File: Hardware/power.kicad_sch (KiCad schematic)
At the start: 0 parts

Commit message: CSG325?
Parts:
- added U2: XC7A35T-CSG325, Package_BGA:Xilinx_CSG325, symbol FPGA_Xilinx_Artix7:XC7A35T-CSG325

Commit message: Found the global labels
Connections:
- net GND: now reaches U2.A1 (GND)
- net GND: now also U2.A11 (GND), U2.A18 (GND), U2.A5 (GND), U2.A7 (GND), U2.A8 (GND), U2.B18 (GND), U2.B3 (GND), U2.B7 (GND), U2.B8 (GND), U2.C15 (GND), U2.C2 (GND), U2.C6 (GND), U2.C7 (GND), U2.D12 (GND), U2.D3 (GND), U2.D4 (GND), U2.D7 (GND), U2.E2 (GND), U2.E6 (GND), U2.E7 (GND), U2.E9 (GND), U2.F10 (GND), U2.F16 (GND), U2.F4 (GND), U2.F6 (GND), U2.G1 (GND), U2.G11 (GND), U2.G13 (GND), U2.G5 (GND), U2.G6 (GND), U2.G7 (GND), U2.G9 (GND), U2.H10 (GND), U2.H12 (GND), U2.H3 (GND), U2.H4 (GND), U2.H5 (GND), U2.H6 (GND), U2.H8 (GND), U2.J1 (GND), U2.J11 (GND), U2.J13 (GND), U2.J17 (GND), U2.J2 (GND), U2.J3 (GND), U2.J7 (GND), U2.J9 (GNDADC_0), U2.K12 (GND), U2.K14 (GND), U2.K4 (GND), U2.K8 (GND), U2.L1 (GND), U2.L11 (GND), U2.L13 (GND), U2.L7 (GND), U2.M12 (GND), U2.M18 (GND), U2.M8 (GND), U2.N11 (GND), U2.N13 (GND), U2.N15 (GND), U2.N5 (GND), U2.N7 (GND), U2.N9 (GND), U2.P12 (GND), U2.P2 (GND), U2.P8 (GND), U2.R9 (GND), U2.T16 (GND), U2.T6 (GND), U2.U13 (GND), U2.U3 (GND), U2.V1 (GND), U2.V10 (GND), U2.V18 (GND)
- net +1V8: now reaches U2.E11 (VCCBATT_0)
- net +1V8: now also U2.G12 (VCCAUX), U2.H13 (VCCAUX), U2.J10 (VCCADC_0), U2.K13 (VCCAUX), U2.M13 (VCCAUX), U2.P13 (VCCAUX)
- net +1V0: now reaches U2.F11 (VCCBRAM)
- net +1V0: now also U2.F7 (VCCINT), U2.F9 (VCCINT), U2.G10 (VCCBRAM), U2.G8 (VCCINT), U2.H11 (VCCBRAM), U2.H7 (VCCINT), U2.H9 (VCCINT), U2.J12 (VCCINT), U2.J8 (VCCINT), U2.K11 (VCCINT), U2.K7 (VCCINT), U2.L12 (VCCINT), U2.L8 (VCCINT), U2.M11 (VCCINT), U2.M7 (VCCINT), U2.N10 (VCCINT), U2.N12 (VCCINT), U2.N8 (VCCINT), U2.P11 (VCCINT), U2.P9 (VCCINT)

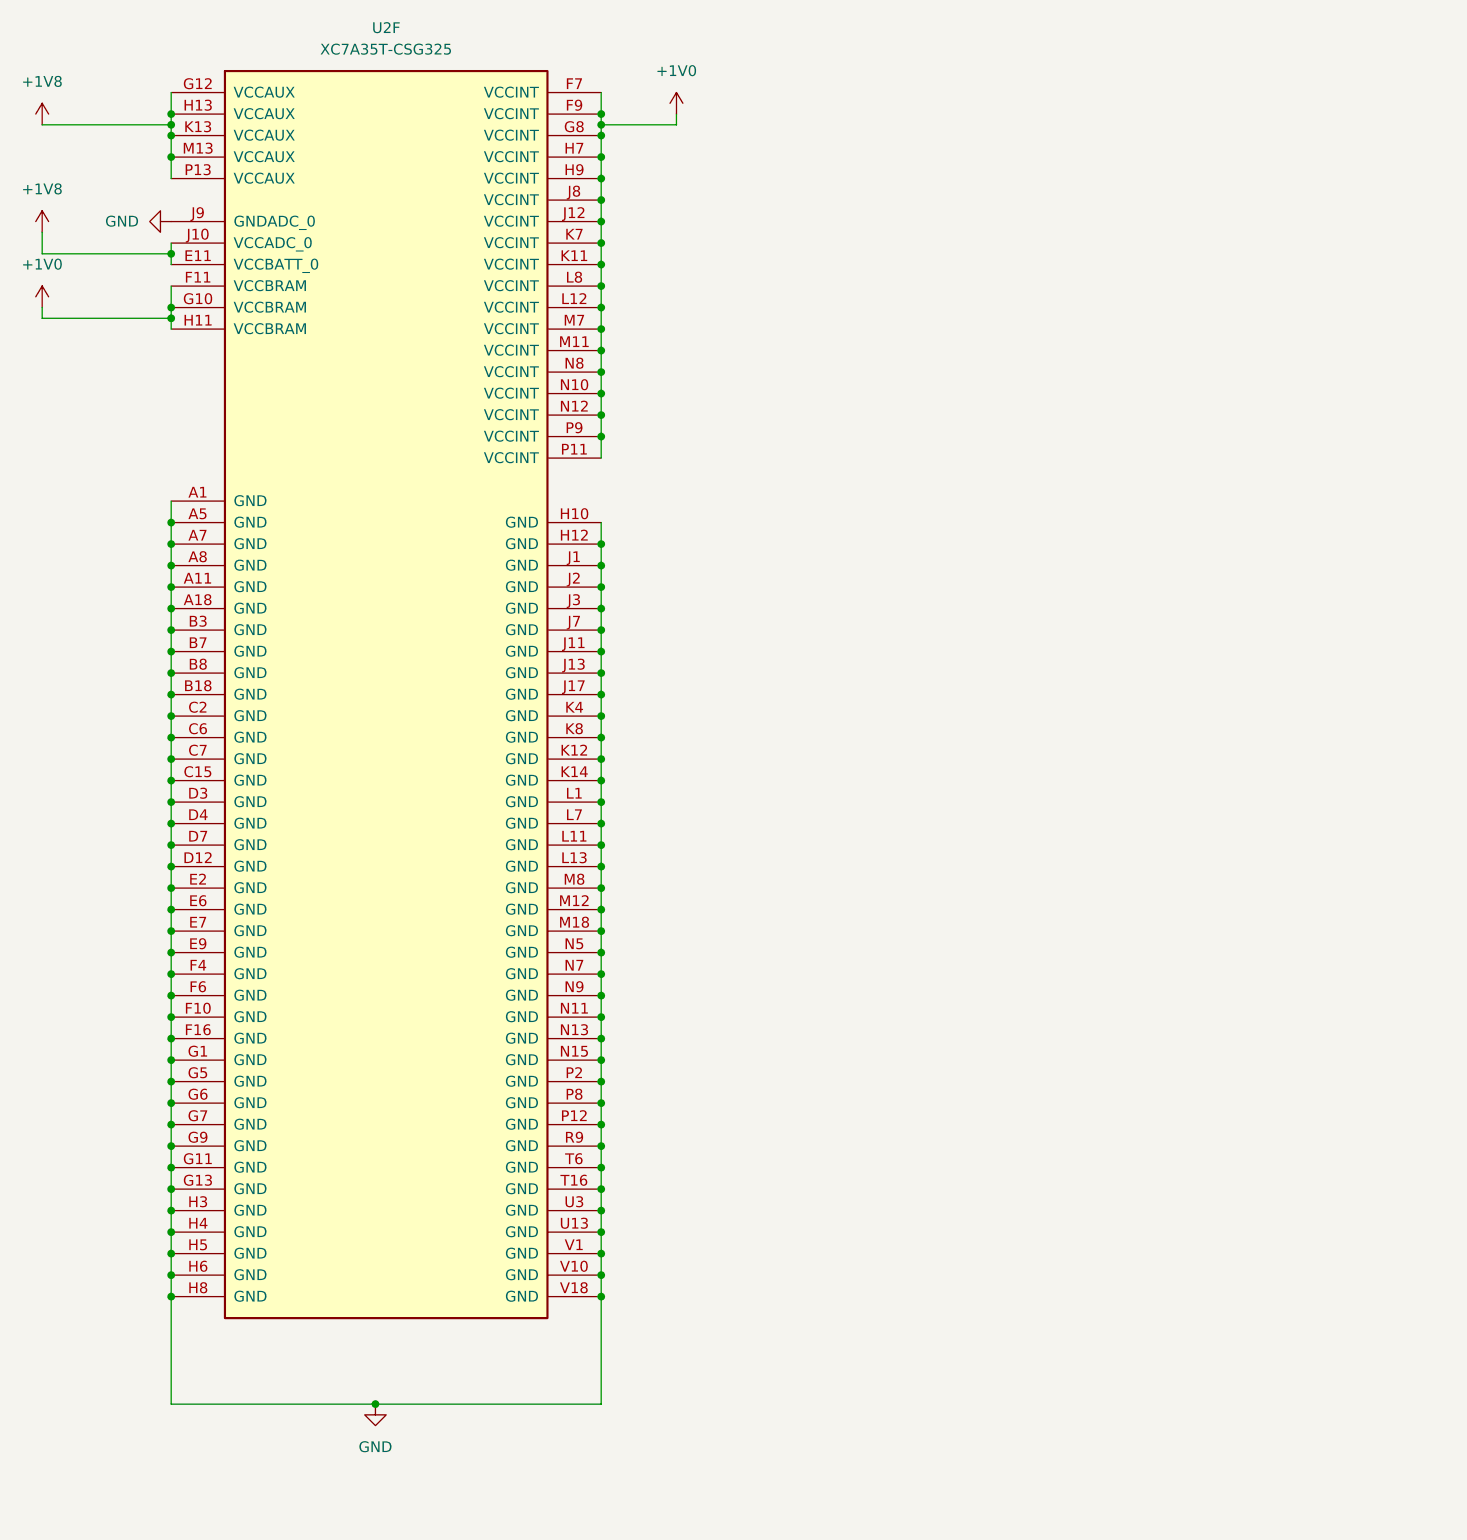
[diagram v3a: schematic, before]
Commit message: Filling out the JTAG
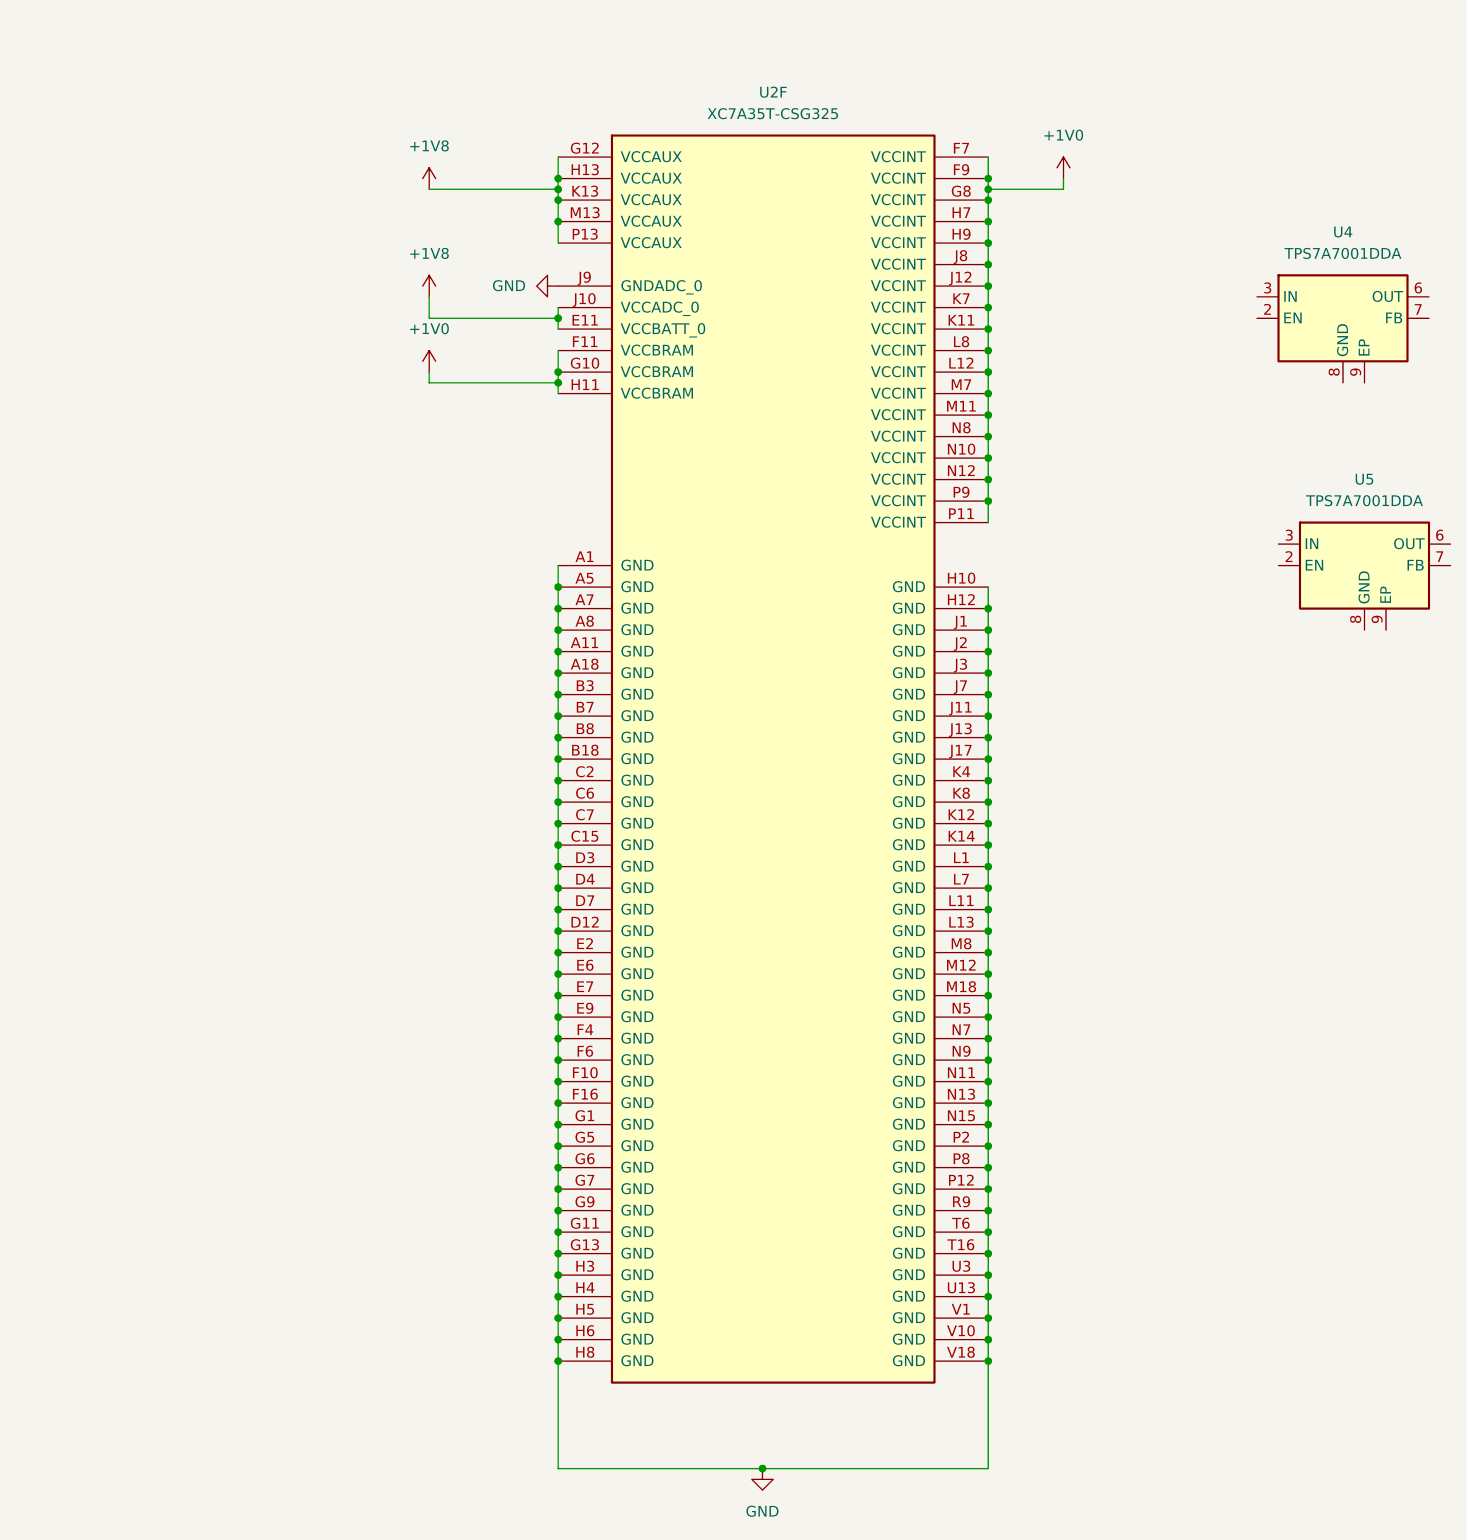
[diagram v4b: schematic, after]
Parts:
- added U4, U5: TPS7A7001DDA, Package_SO:TI_SO-PowerPAD-8, symbol Regulator_Linear:TPS7A7001DDA
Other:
- moved on the sheet: U2F
